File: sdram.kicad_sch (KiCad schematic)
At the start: 5 parts, among them U1 ECP5U_12_CABGA256, U10 W9825G6KH-6

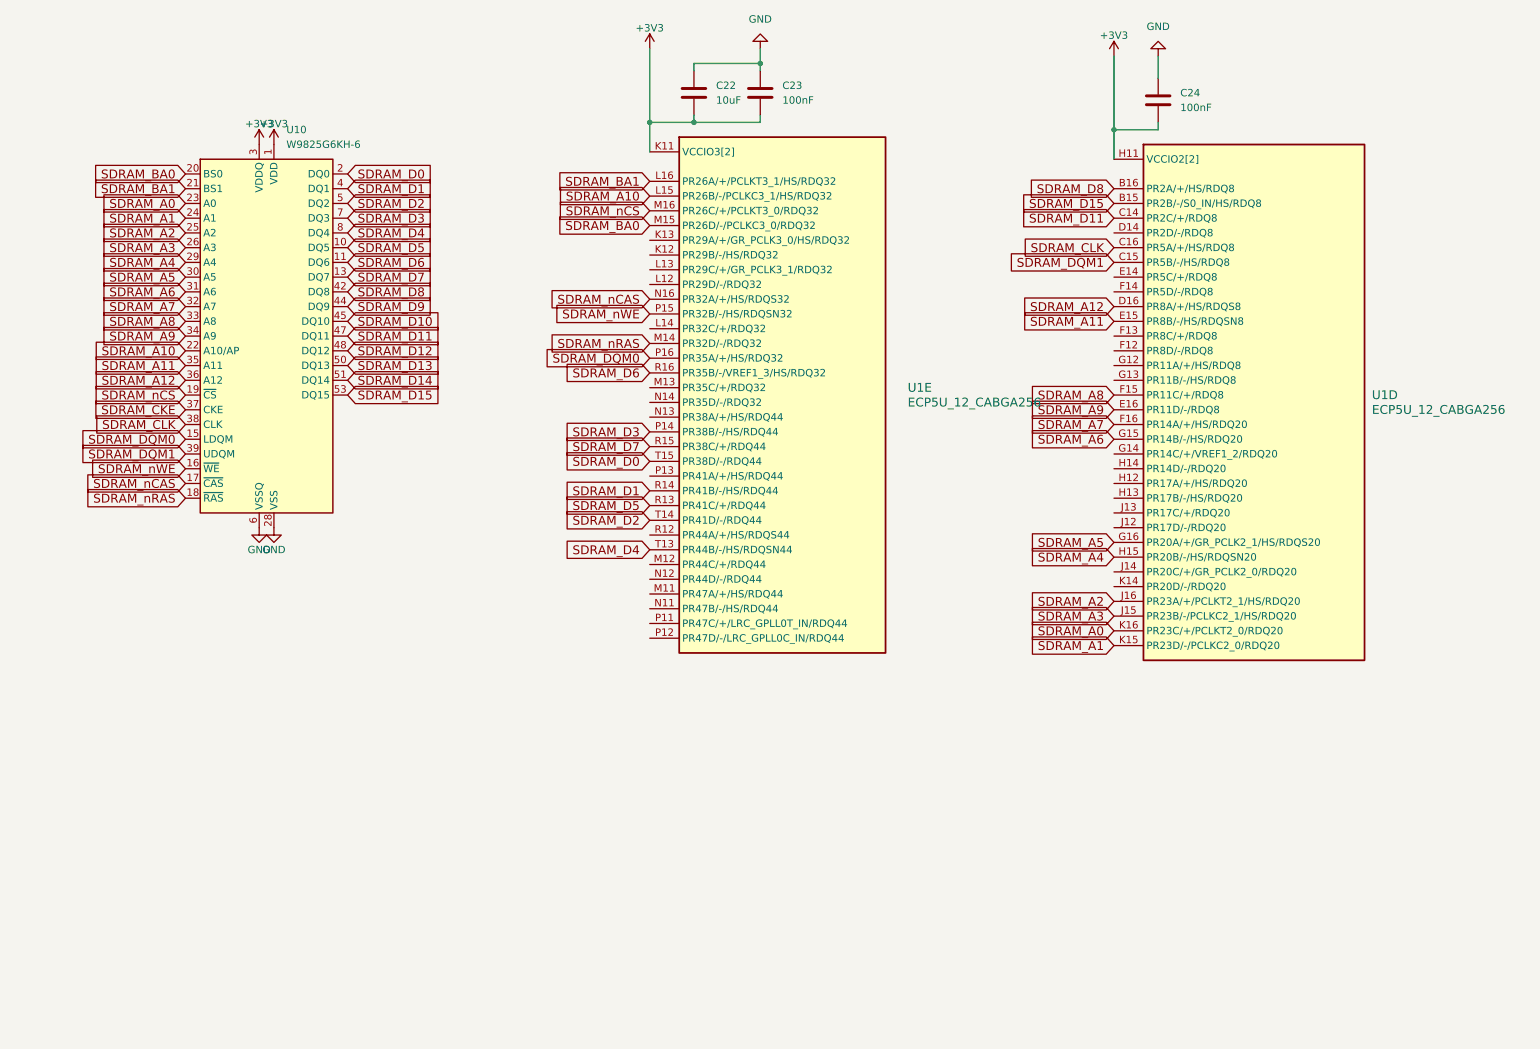
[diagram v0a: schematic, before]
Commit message: Routed HDMI, usb, rotated chip and more
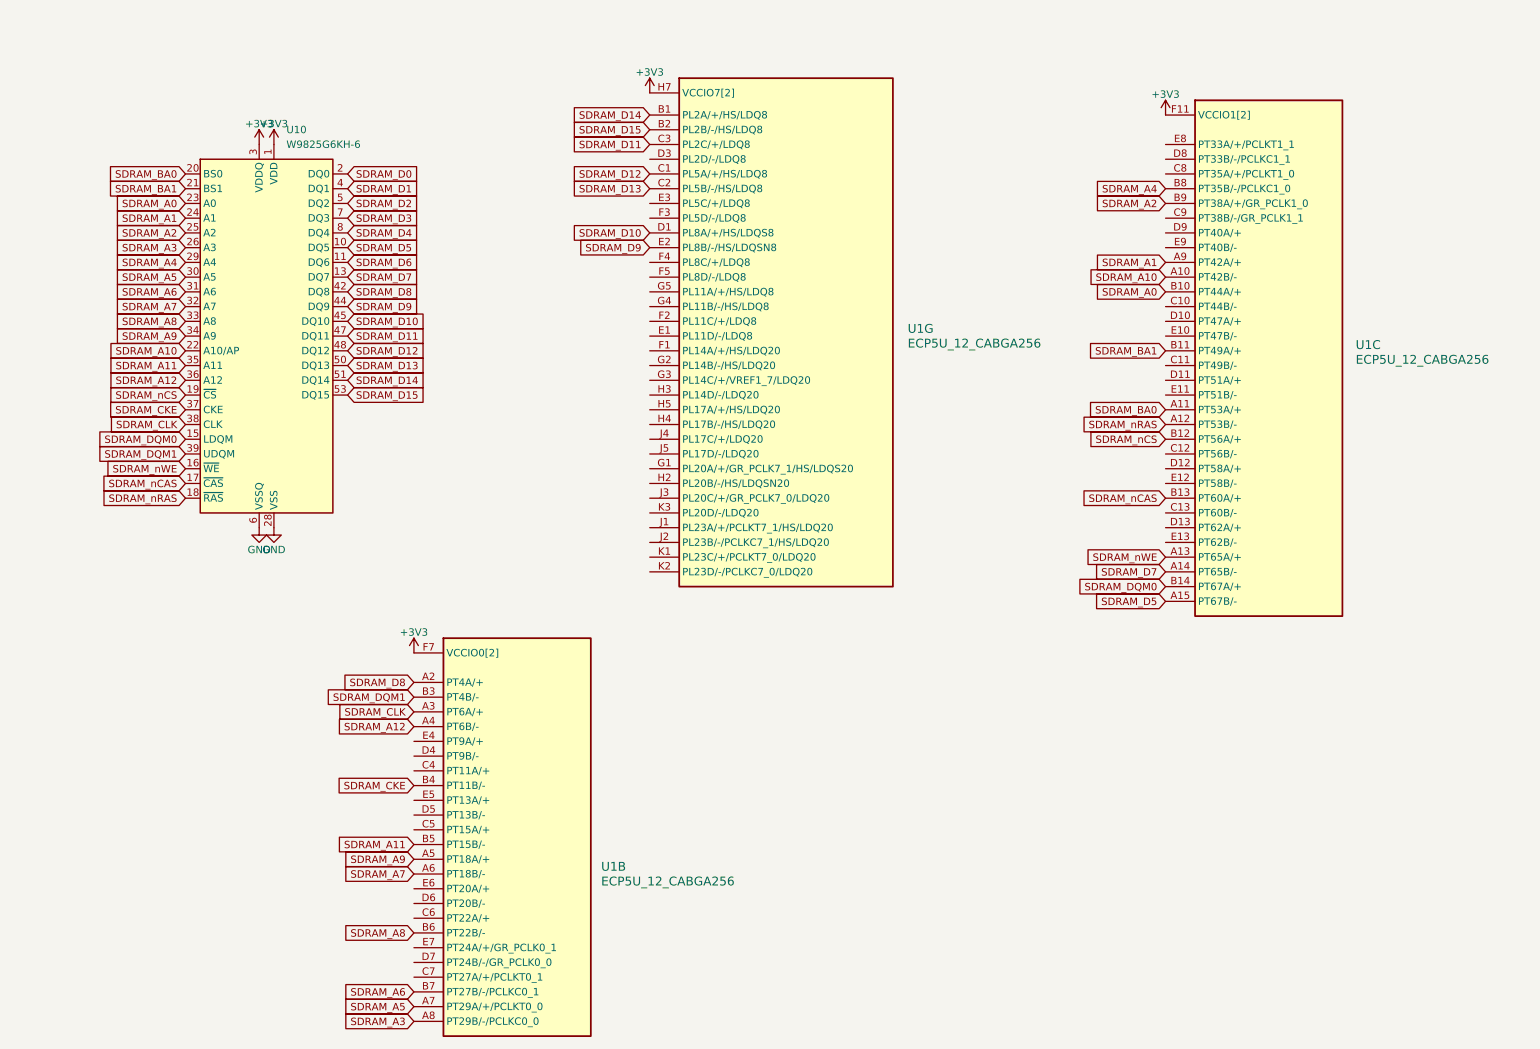
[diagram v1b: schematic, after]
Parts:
- removed C22: 10uF, Capacitor_SMD:C_0603_1608Metric, symbol Device:C
- removed C23, C24: 100nF, Capacitor_SMD:C_0402_1005Metric, symbol Device:C
- removed U1: ECP5U_12_CABGA256, Package_BGA:BGA-256_14.0x14.0mm_Layout16x16_P0.8mm_Ball0.45mm_Pad0.32mm_NSMD, symbol josh-ic:ECP5U_12_CABGA256
- added U1: ECP5U_12_CABGA256, Package_BGA:BGA-256_14.0x14.0mm_Layout16x16_P0.8mm_Ball0.45mm_Pad0.32mm_NSMD, symbol josh-ic:ECP5U_12_CABGA256
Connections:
- net +3V3: now also U1.F10 (VCCIO1[2]), U1.F11 (VCCIO1[2]), U1.F6 (VCCIO0[2]), U1.F7 (VCCIO0[2]), U1.H6 (VCCIO7[2]), U1.H7 (VCCIO7[2])
- net SDRAM_A0: now also U1.B10 (PT44A/+)
- net SDRAM_A1: now also U1.A9 (PT42A/+)
- net SDRAM_A10: now also U1.A10 (PT42B/-)
- net SDRAM_A11: now also U1.B5 (PT15B/-)
- net SDRAM_A12: now also U1.A4 (PT6B/-)
- net SDRAM_A2: now also U1.B9 (PT38A/+/GR_PCLK1_0)
- net SDRAM_A3: now also U1.A8 (PT29B/-/PCLKC0_0)
- net SDRAM_A4: now also U1.B8 (PT35B/-/PCLKC1_0)
- net SDRAM_A5: now also U1.A7 (PT29A/+/PCLKT0_0)
- net SDRAM_A6: now also U1.B7 (PT27B/-/PCLKC0_1)
- net SDRAM_A7: now also U1.A6 (PT18B/-)
- net SDRAM_A8: now also U1.B6 (PT22B/-)
- net SDRAM_A9: now also U1.A5 (PT18A/+)
- net SDRAM_BA0: now also U1.A11 (PT53A/+)
- net SDRAM_BA1: now also U1.B11 (PT49A/+)
- net SDRAM_CKE: now also U1.B4 (PT11B/-)
- net SDRAM_CLK: now also U1.A3 (PT6A/+)
- net SDRAM_D10: now also U1.D1 (PL8A/+/HS/LDQS8)
- net SDRAM_D11: now also U1.C3 (PL2C/+/LDQ8)
- net SDRAM_D12: now also U1.C1 (PL5A/+/HS/LDQ8)
- net SDRAM_D13: now also U1.C2 (PL5B/-/HS/LDQ8)
- net SDRAM_D14: now also U1.B1 (PL2A/+/HS/LDQ8)
- net SDRAM_D15: now also U1.B2 (PL2B/-/HS/LDQ8)
- net SDRAM_D5: now also U1.A15 (PT67B/-)
- net SDRAM_D7: now also U1.A14 (PT65B/-)
- net SDRAM_D8: now also U1.A2 (PT4A/+)
- net SDRAM_D9: now also U1.E2 (PL8B/-/HS/LDQSN8)
- net SDRAM_DQM0: now also U1.B14 (PT67A/+)
- net SDRAM_DQM1: now also U1.B3 (PT4B/-)
- net SDRAM_nCAS: now also U1.B13 (PT60A/+)
- net SDRAM_nCS: now also U1.B12 (PT56A/+)
- net SDRAM_nRAS: now also U1.A12 (PT53B/-)
- net SDRAM_nWE: now also U1.A13 (PT65A/+)

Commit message: Stash
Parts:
- added C30, C32: 10uF, Capacitor_SMD:C_0603_1608Metric, symbol Device:C
- added C31, C33, C34, C35: 100nF, Capacitor_SMD:C_0402_1005Metric, symbol Device:C
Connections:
- net +3V3: now also C30.2, C31.2, C32.2, C33.2, C34.2, C35.2
- net GND: now also C30.1, C31.1, C32.1, C33.1, C34.1, C35.1
- net CONN40: now reaches U1.E1 (PL11D/-/LDQ8)
- net CONN37: now reaches U1.E3 (PL5C/+/LDQ8)
- net CONN35: now reaches U1.F1 (PL14A/+/HS/LDQ20)
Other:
- moved on the sheet: U10, U1B, U1C, U1G

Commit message: Rev 1
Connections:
- net CONN33: now reaches U1.E4 (PT9A/+)
- net CONN38: now reaches U1.F2 (PL11C/+/LDQ8)
- net CONN27: now reaches U1.F3 (PL5D/-/LDQ8)
- net CONN29: now reaches U1.F4 (PL8C/+/LDQ8)
- net CONN36: now reaches U1.G1 (PL20A/+/GR_PCLK7_1/HS/LDQS20)
- net CONN31: now reaches U1.G2 (PL14B/-/HS/LDQ20)
- net CONN32: now reaches U1.J1 (PL23A/+/PCLKT7_1/HS/LDQ20)
- net CONN23: now reaches U1.J2 (PL23B/-/PCLKC7_1/HS/LDQ20)
- net CONN28: now reaches U1.K1 (PL23C/+/PCLKT7_0/LDQ20)
- net CONN26: now reaches U1.K2 (PL23D/-/PCLKC7_0/LDQ20)
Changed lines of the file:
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@@
+		)
+	)
+	(global_label "CONN33"
+		(shape input)
+		(at 41.91 139.7 180)
+		(fields_autoplaced yes)
+		(effects
+			(font
+				(size 1.27 1.27)
+			)
+			(justify right)
+		)
+		(property "Intersheetrefs" "${INTERSHEET_REFS}"
+			(at 31.2443 139.7 0)
+			(effects
+				(font
+					(size 1.27 1.27)
+				)
+				(justify right)
+				(hide yes)
+			)
 		)
 	)
@@
 		)
 	)
+	(global_label "CONN26"
+		(shape input)
+		(at 114.3 129.54 180)
+		(fields_autoplaced yes)
+		(effects
+			(font
+				(size 1.27 1.27)
+			)
+			(justify right)
+		)
+		(property "Intersheetrefs" "${INTERSHEET_REFS}"
+			(at 103.6343 129.54 0)
+			(effects
+				(font
+					(size 1.27 1.27)
+				)
+				(justify right)
+				(hide yes)
+			)
+		)
+	)
 	(global_label "CONN35"
 		(shape input)
@@
 		)
 	)
+	(global_label "CONN38"
+		(shape input)
+		(at 114.3 86.36 180)
+		(fields_autoplaced yes)
+		(effects
+			(font
+				(size 1.27 1.27)
+			)
+			(justify right)
+		)
+		(property "Intersheetrefs" "${INTERSHEET_REFS}"
+			(at 103.6343 86.36 0)
+			(effects
+				(font
+					(size 1.27 1.27)
+				)
+				(justify right)
+				(hide yes)
+			)
+		)
+	)
 	(global_label "SDRAM_nCAS"
 		(shape input)
@@
 					(bold yes)
 				)
+				(hide yes)
+			)
+		)
+	)
+	(global_label "CONN32"
+		(shape input)
+		(at 114.3 121.92 180)
+		(fields_autoplaced yes)
+		(effects
+			(font
+				(size 1.27 1.27)
+			)
+			(justify right)
+		)
+		(property "Intersheetrefs" "${INTERSHEET_REFS}"
+			(at 103.6343 121.92 0)
+			(effects
+				(font
+					(size 1.27 1.27)
+				)
+				(justify right)
 				(hide yes)
 			)
@@
 		)
 	)
+	(global_label "CONN27"
+		(shape input)
+		(at 114.3 68.58 180)
+		(fields_autoplaced yes)
+		(effects
+			(font
+				(size 1.27 1.27)
+			)
+			(justify right)
+		)
+		(property "Intersheetrefs" "${INTERSHEET_REFS}"
+			(at 103.6343 68.58 0)
+			(effects
+				(font
+					(size 1.27 1.27)
+				)
+				(justify right)
+				(hide yes)
+			)
+		)
+	)
 	(global_label "SDRAM_D14"
 		(shape input)
@@
 					(bold yes)
 				)
+				(hide yes)
+			)
+		)
+	)
+	(global_label "CONN23"
+		(shape input)
+		(at 114.3 124.46 180)
+		(fields_autoplaced yes)
+		(effects
+			(font
+				(size 1.27 1.27)
+			)
+			(justify right)
+		)
+		(property "Intersheetrefs" "${INTERSHEET_REFS}"
+			(at 103.6343 124.46 0)
+			(effects
+				(font
+					(size 1.27 1.27)
+				)
+				(justify right)
 				(hide yes)
 			)
@@
 		)
 	)
+	(global_label "CONN28"
+		(shape input)
+		(at 114.3 127 180)
+		(fields_autoplaced yes)
+		(effects
+			(font
+				(size 1.27 1.27)
+			)
+			(justify right)
+		)
+		(property "Intersheetrefs" "${INTERSHEET_REFS}"
+			(at 103.6343 127 0)
+			(effects
+				(font
+					(size 1.27 1.27)
+				)
+				(justify right)
+				(hide yes)
+			)
+		)
+	)
+	(global_label "CONN36"
+		(shape input)
+		(at 114.3 111.76 180)
+		(fields_autoplaced yes)
+		(effects
+			(font
+				(size 1.27 1.27)
+			)
+			(justify right)
+		)
+		(property "Intersheetrefs" "${INTERSHEET_REFS}"
+			(at 103.6343 111.76 0)
+			(effects
+				(font
+					(size 1.27 1.27)
+				)
+				(justify right)
+				(hide yes)
+			)
+		)
+	)
 	(global_label "SDRAM_D15"
 		(shape input)
@@
 		)
 	)
+	(global_label "CONN31"
+		(shape input)
+		(at 114.3 93.98 180)
+		(fields_autoplaced yes)
+		(effects
+			(font
+				(size 1.27 1.27)
+			)
+			(justify right)
+		)
+		(property "Intersheetrefs" "${INTERSHEET_REFS}"
+			(at 103.6343 93.98 0)
+			(effects
+				(font
+					(size 1.27 1.27)
+				)
+				(justify right)
+				(hide yes)
+			)
+		)
+	)
 	(global_label "SDRAM_CKE"
 		(shape input)
@@
 				(hide yes)
 			)
+		)
+	)
+	(global_label "CONN29"
+		(shape input)
+		(at 114.3 76.2 180)
+		(fields_autoplaced yes)
+		(effects
+			(font
+				(size 1.27 1.27)
+			)
+			(justify right)
+		)
+		(property "Intersheetrefs" "${INTERSHEET_REFS}"
+			(at 103.6343 76.2 0)
+			(effects
+				(font
+					(size 1.27 1.27)
+				)
+				(justify right)
+				(hide yes)
+			)
